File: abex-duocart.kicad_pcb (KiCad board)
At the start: 2 copper layers, 135.5 x 71.5 mm, 52 parts, among them J1 Micro_SD_Card_Det, P1 0877159106, P2 CONN_01X01, P3 CONN_01X01, P4 CONN_01X01, P5 CONN_01X01, SW2 SW_Push, U1 STM32F407VGTx

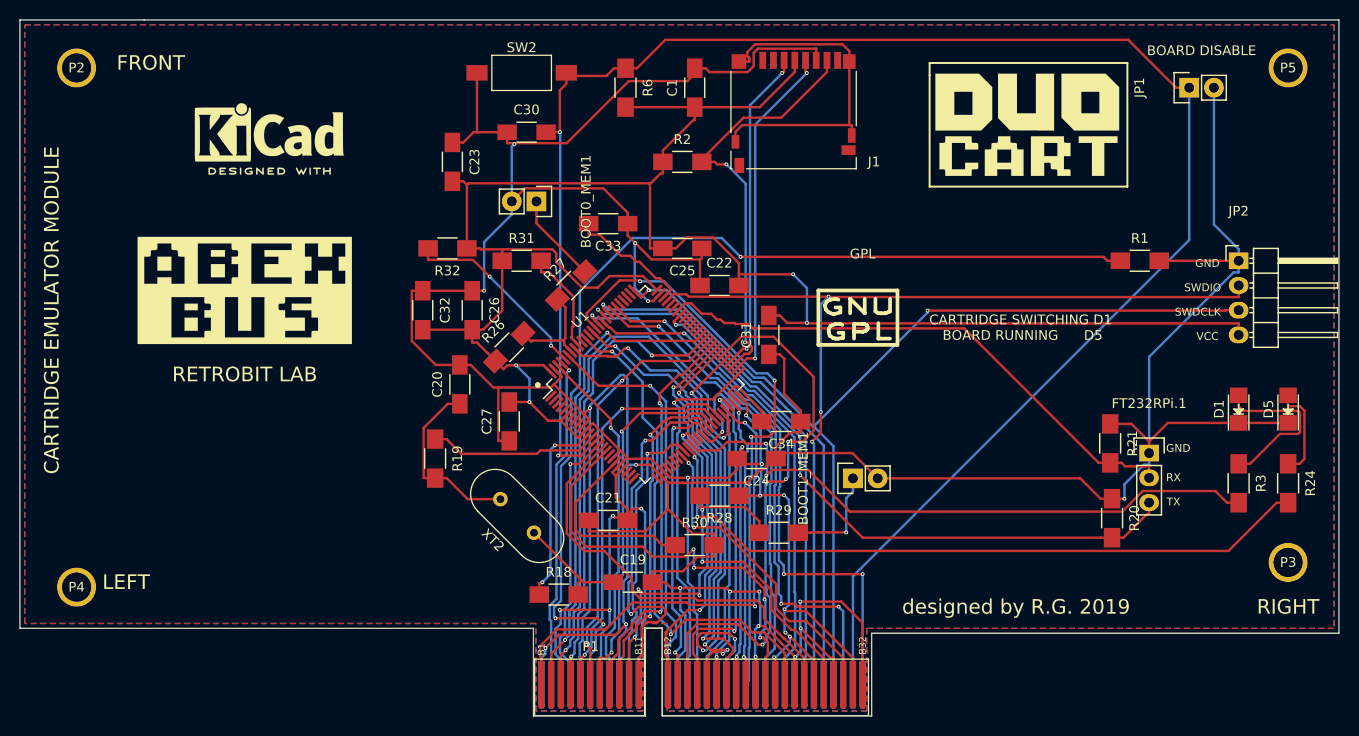
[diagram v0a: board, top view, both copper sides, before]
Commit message: Corrected some silkscreen bugs
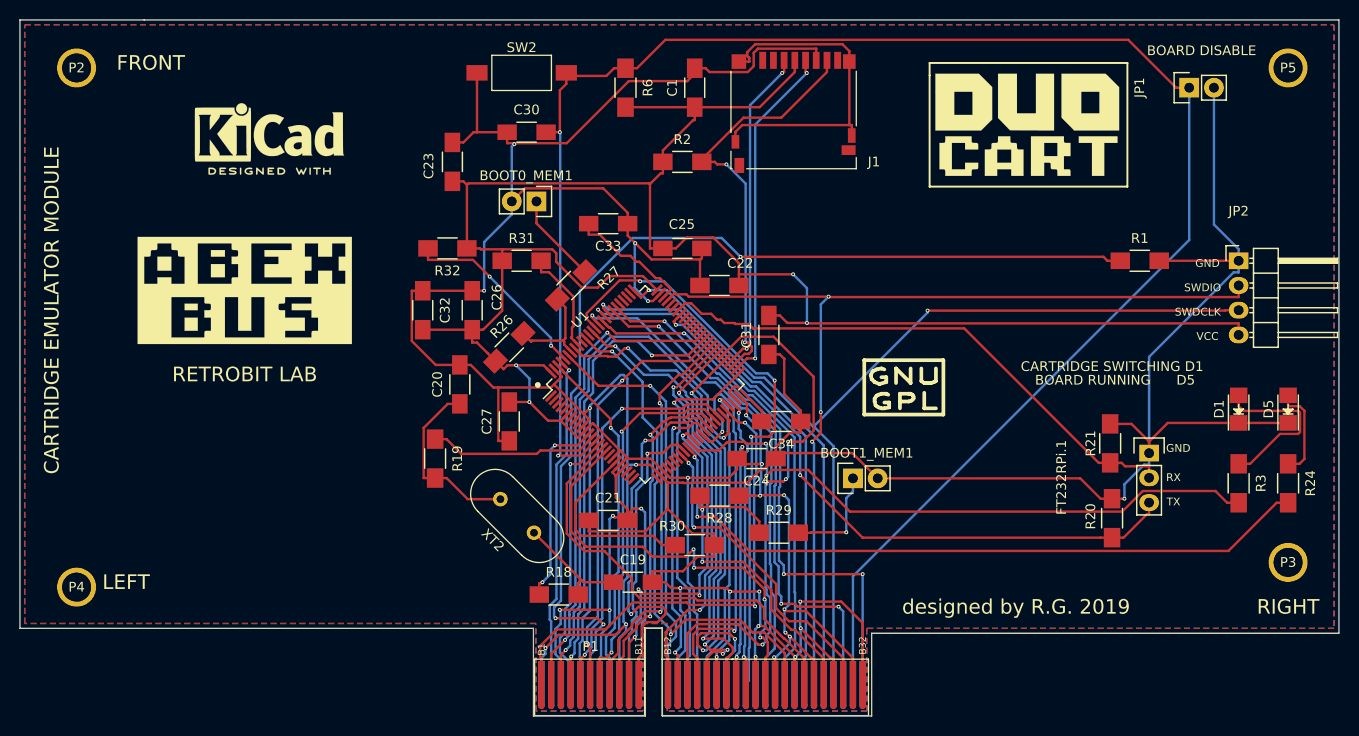
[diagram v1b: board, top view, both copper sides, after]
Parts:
- moved GPL 8.58 mm to (168.8, 92.0)
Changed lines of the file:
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@@
     (links 159)
     (no_connects 0)
-    (area 57.500001 40.65 239.285715 134.350001)
+    (area 77.949999 53.949999 213.550001 125.550001)
     (thickness 1.6)
     (drawings 48)
@@
   )
   (module RetroBitLab:Symbol_GNU-GPL_SilkScreen_Small (layer F.Cu)
-    (at 164.084 84.836)
+    (at 168.8 92)
     (descr "Symbol, GNU-GPL, Copper Top, Small,")
     (tags "Symbol, GNU-GPL, Copper Top, Small,")
-    (fp_text reference GPL (at 0.50038 -6.79958) (layer F.SilkS)
+    (fp_text reference GPL (at 0.50038 -6.79958) (layer F.SilkS) hide
       (effects (font (size 1 1) (thickness 0.15)))
     )
@@
     (tags "resistor 1206")
     (attr smd)
-    (fp_text reference R30 (at 0 -2.3) (layer F.SilkS)
+    (fp_text reference R30 (at -2.32 -1.95) (layer F.SilkS)
       (effects (font (size 1 1) (thickness 0.15)))
     )
@@
     (tags "resistor 1206")
     (attr smd)
-    (fp_text reference R27 (at 0 -2.3 45) (layer F.SilkS)
+    (fp_text reference R27 (at 3.295118 2.192031 45) (layer F.SilkS)
       (effects (font (size 1 1) (thickness 0.15)))
     )
@@
     (tags "resistor 1206")
     (attr smd)
-    (fp_text reference R26 (at 0 -2.3 45) (layer F.SilkS)
+    (fp_text reference R26 (at 0.961665 -2.05061 45) (layer F.SilkS)
       (effects (font (size 1 1) (thickness 0.15)))
     )
@@
     (tags "resistor 1206")
     (attr smd)
-    (fp_text reference R21 (at 0 -2.3 270) (layer F.SilkS)
+    (fp_text reference R21 (at 0 2 270) (layer F.SilkS)
       (effects (font (size 1 1) (thickness 0.15)))
     )
@@
     (tags "resistor 1206")
     (attr smd)
-    (fp_text reference R20 (at 0 -2.3 270) (layer F.SilkS)
+    (fp_text reference R20 (at -0.185 2.195 270) (layer F.SilkS)
       (effects (font (size 1 1) (thickness 0.15)))
     )
@@
     (descr "Through hole pin header")
     (tags "pin header")
-    (fp_text reference FT232RPi.1 (at 0 -5.1) (layer F.SilkS)
+    (fp_text reference FT232RPi.1 (at -9 2.5 90) (layer F.SilkS)
       (effects (font (size 1 1) (thickness 0.15)))
     )
@@
     (tags "capacitor 1206")
     (attr smd)
-    (fp_text reference C26 (at 0 -2.3 270) (layer F.SilkS)
+    (fp_text reference C26 (at -1.32 -2.54 270) (layer F.SilkS)
       (effects (font (size 1 1) (thickness 0.15)))
     )
@@
     (tags "capacitor 1206")
     (attr smd)
-    (fp_text reference C25 (at 0 -2.3 180) (layer F.SilkS)
+    (fp_text reference C25 (at 0.05 2.47 180) (layer F.SilkS)
       (effects (font (size 1 1) (thickness 0.15)))
     )
@@
     (tags "capacitor 1206")
     (attr smd)
-    (fp_text reference C23 (at 0 -2.3 270) (layer F.SilkS)
+    (fp_text reference C23 (at 0.42 2.428 270) (layer F.SilkS)
       (effects (font (size 1 1) (thickness 0.15)))
     )
@@
     (tags "capacitor 1206")
     (attr smd)
-    (fp_text reference C22 (at 0 -2.3) (layer F.SilkS)
+    (fp_text reference C22 (at 2.14 -2.28) (layer F.SilkS)
       (effects (font (size 1 1) (thickness 0.15)))
     )
@@
     (descr "Through hole pin header")
     (tags "pin header")
-    (fp_text reference BOOT1_MEM1 (at 0 -5.1 90) (layer F.SilkS)
+    (fp_text reference BOOT1_MEM1 (at 2.592 1.424 180) (layer F.SilkS)
       (effects (font (size 1 1) (thickness 0.15)))
     )
@@
     (descr "Through hole pin header")
     (tags "pin header")
-    (fp_text reference BOOT0_MEM1 (at 0 -5.1 270) (layer F.SilkS)
+    (fp_text reference BOOT0_MEM1 (at -2.644 1.064 360) (layer F.SilkS)
       (effects (font (size 1 1) (thickness 0.15)))
     )
@@
     (arrow2b (pts (xy 232 117) (xy 232.586421 118.126504)))
   )
-  (gr_text "BOARD RUNNING      D5" (at 181 86.4) (layer F.SilkS)
+  (gr_text "BOARD RUNNING      D5" (at 190.5 91) (layer F.SilkS)
     (effects (font (size 1 1) (thickness 0.2)))
   )
-  (gr_text "CARTRIDGE SWITCHING D1" (at 180.8 84.8) (layer F.SilkS)
+  (gr_text "CARTRIDGE SWITCHING D1" (at 190.2 89.6) (layer F.SilkS)
     (effects (font (size 1 1) (thickness 0.2)))
   )

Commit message: Added the CardDetect. Added the A31 +5V pin
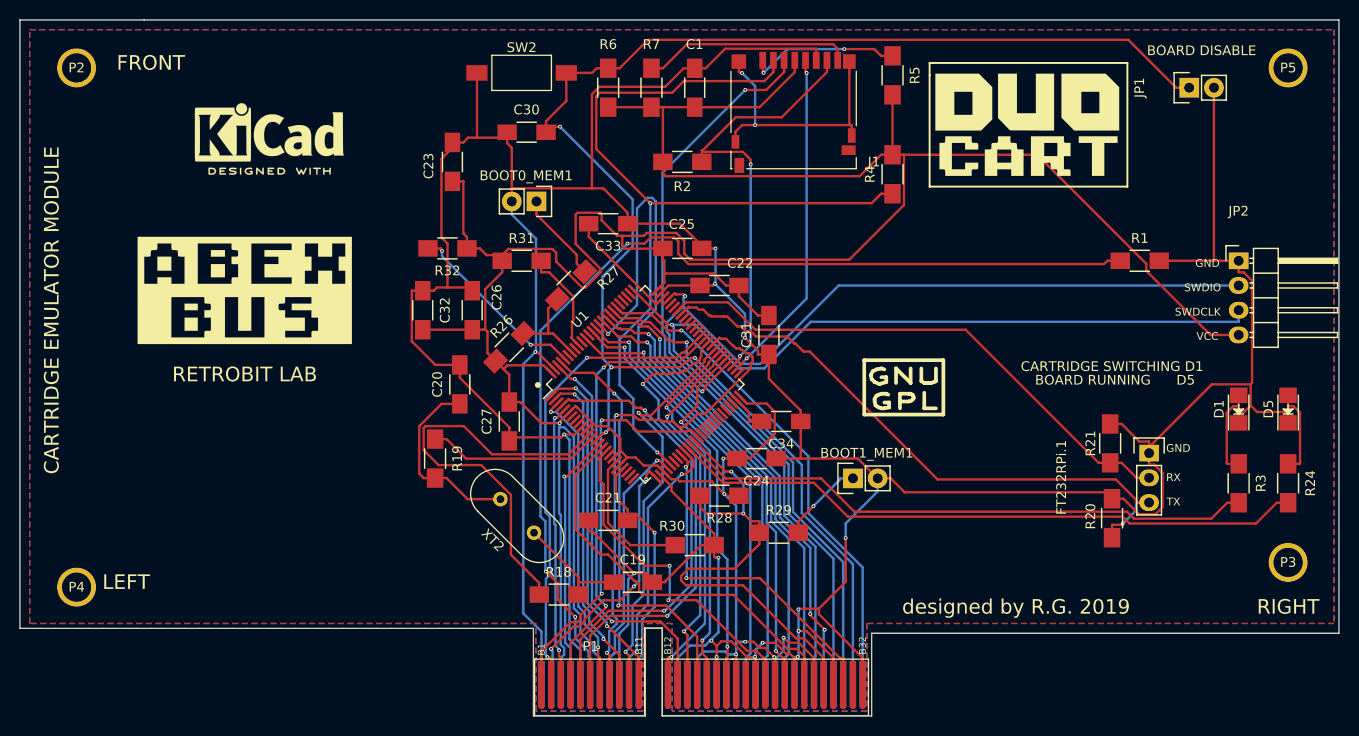
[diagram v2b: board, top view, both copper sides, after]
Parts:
- added R4: 4.7K, Resistors_SMD:R_1206_HandSoldering, F.Cu at (167.6, 69.8)
- added R5: 4.7K, Resistors_SMD:R_1206_HandSoldering, F.Cu at (167.6, 59.7)
- added R7: 4.7K, Resistors_SMD:R_1206_HandSoldering, F.Cu at (142.9, 61.0)
- moved R6 1.78 mm to (138.4, 61.0)
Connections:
- J1 pad 1: (no net) -> Net-(J1-Pad1)
- J1 pad 2: (no net) -> mCD
- J1 pad 8: (no net) -> Net-(J1-Pad8)
- P1 pad A12: ~mEXSEL -> (no net)
- P1 pad A14: ~mIRQ -> (no net)
- P1 pad A16: ~mHALT -> (no net)
- P1 pad A18: ~mD1XX -> (no net)
- P1 pad A20: ~mMPD -> (no net)
- P1 pad A31: VCC_3V3 -> (no net)
- U1 pad 1: (no net) -> mD2
- U1 pad 2: (no net) -> mD3
- U1 pad 26: (no net) -> ~mRST
- U1 pad 29: (no net) -> ~mREF
- U1 pad 3: (no net) -> mD4
- U1 pad 30: (no net) -> mCD
- U1 pad 38: (no net) -> mD7
- U1 pad 39: mD0 -> (no net)
- U1 pad 4: (no net) -> mD5
- U1 pad 40: mD1 -> (no net)
- U1 pad 41: mD2 -> (no net)
- U1 pad 42: mD3 -> (no net)
- U1 pad 43: mD4 -> (no net)
- U1 pad 44: mD5 -> (no net)
- U1 pad 45: mD6 -> (no net)
- U1 pad 46: mD7 -> (no net)
- U1 pad 47: ~mHALT -> (no net)
- U1 pad 48: ~mMPD -> (no net)
- U1 pad 5: (no net) -> mD6
- U1 pad 51: ~mIRQ -> (no net)
- U1 pad 93: ~mD1XX -> (no net)
- U1 pad 95: ~mEXSEL -> (no net)
- U1 pad 97: ~mRST -> mD0
- U1 pad 98: ~mREF -> mD1
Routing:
- net mCD: track 0.00 -> 89.4 mm, vias 0 -> 2
- net ~mD1XX: track 54.9 -> 0.00 mm, vias 3 -> 0
- net ~mEXSEL: track 41.7 -> 0.00 mm, vias 1 -> 0
- net ~mIRQ: track 37.8 -> 0.00 mm, vias 1 -> 0
- net ~mHALT: track 31.8 -> 0.00 mm, vias 1 -> 0
- net ~mMPD: track 29.9 -> 0.00 mm, vias 2 -> 0
- net mD6: track 58.5 -> 29.0 mm
- net SWDRST: track 188.7 -> 162.7 mm, vias 2 -> 4
- net Net-(R18-Pad1): track 20.1 -> 43.7 mm, vias 2 -> 0
- net mA5: track 51.1 -> 73.9 mm
- net Net-(J1-Pad8): track 0.00 -> 21.5 mm
- net mA9: track 58.0 -> 38.3 mm, vias 4 -> 2
- net VCC_3V3: track 394.4 -> 413.5 mm, vias 19 -> 8
- net Net-(J1-Pad1): track 0.00 -> 15.9 mm, vias 0 -> 2
- net mA6: track 60.4 -> 44.5 mm, vias 3 -> 1
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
